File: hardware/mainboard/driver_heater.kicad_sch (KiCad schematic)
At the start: 8 parts, among them J18 Screw_Terminal_01x02, Q1 AGM308MBP, SW9 SW_SPDT

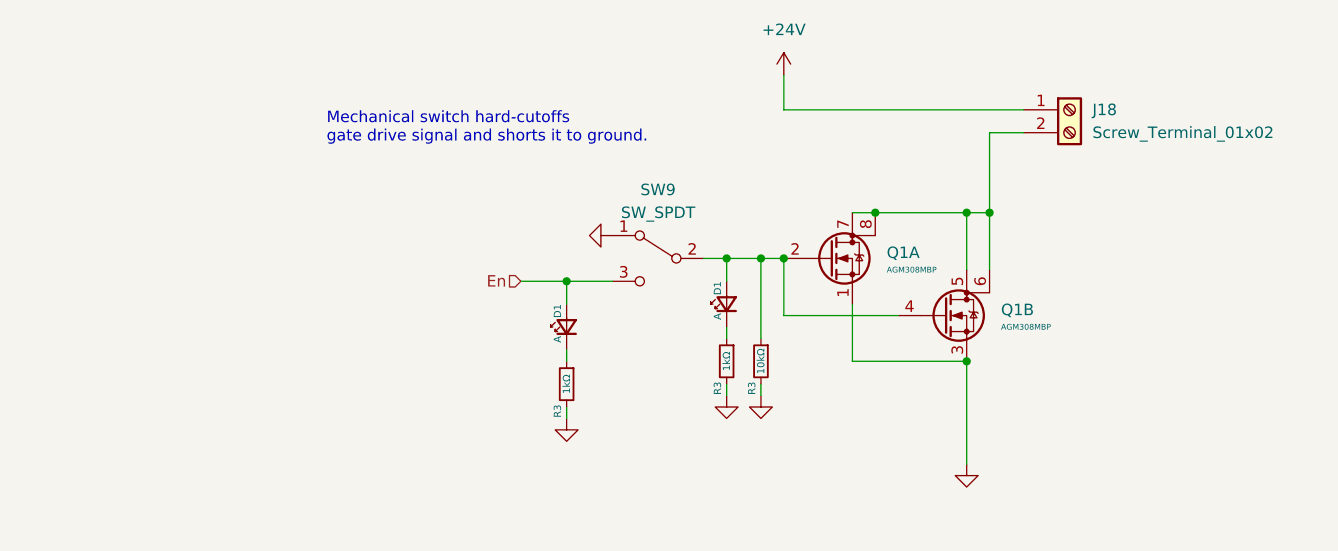
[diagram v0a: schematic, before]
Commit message: saving mainboard, gonna tear out the entire thing and redo in 4-layer
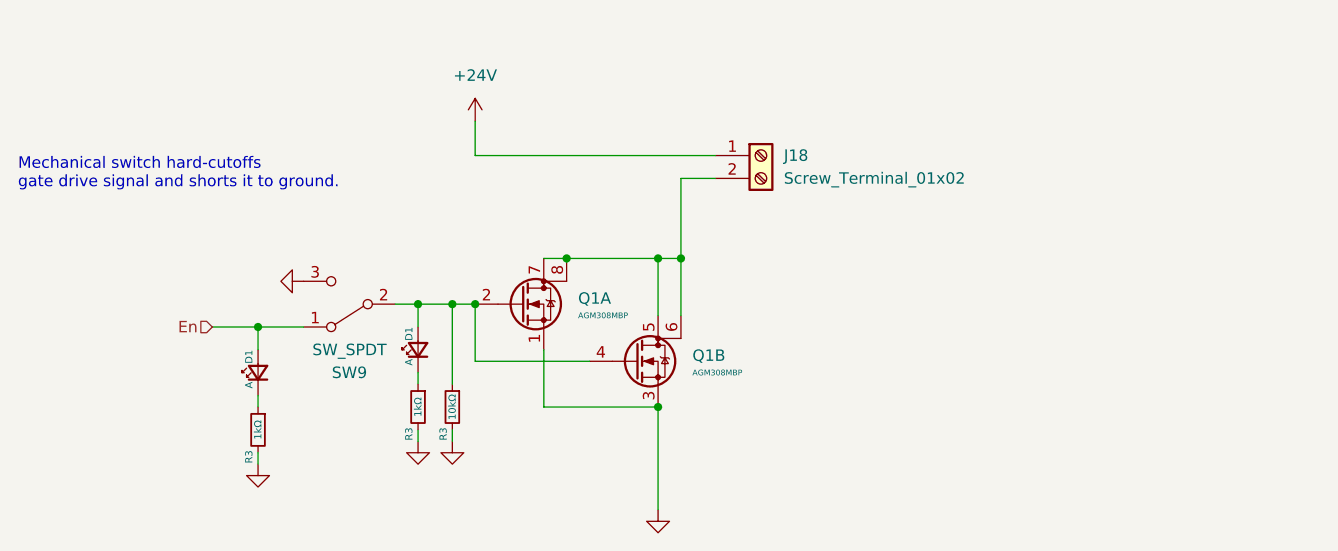
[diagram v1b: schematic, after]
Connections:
- net En: now also SW9.1 (A); no longer SW9.3 (C)
- net GND: now also SW9.3 (C); no longer SW9.1 (A)
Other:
- moved on the sheet: D1, J18, Q1A, Q1B, R3, SW9

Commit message: further board edits, mostly done with power planes, heaters, fans, motor channels, starting work on microcontroller signals
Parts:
- R3: footprint AlphaLib:0603R -> AlphaLib:0402R
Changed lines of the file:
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@@
       (effects (font (size 0.8 0.8)))
     )
-    (property "Footprint" "AlphaLib:0603R" (at 44.45 74.93 0)
+    (property "Footprint" "AlphaLib:0402R" (at 44.45 74.93 0)
       (effects (font (size 1.27 1.27)) hide)
     )
@@
       (effects (font (size 0.8 0.8)))
     )
-    (property "Footprint" "AlphaLib:0603R" (at 66.04 72.39 0)
+    (property "Footprint" "AlphaLib:0402R" (at 66.04 72.39 0)
       (effects (font (size 1.27 1.27)) hide)
     )
@@
       (effects (font (size 0.8 0.8)))
     )
-    (property "Footprint" "AlphaLib:0603R" (at 62.23 72.39 0)
-      (effects (font (size 1.27 1.27)) hide)
-    )
+    (property "Footprint" "AlphaLib:0402R" (at 62.23 72.39 0)
+      (effects (font (size 1.27 1.27)) hide)
+    )

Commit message: redoing board for version alpha 0.2
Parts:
- removed D1 (x2): A, AlphaLib:0603LED, symbol Device:LED_Small
- removed R3 (x2): 1kΩ, AlphaLib:0402R, symbol Device:R_Small
- removed R3: 10kΩ, AlphaLib:0402R, symbol Device:R_Small
- removed SW9: SW_SPDT, corevus:MSS12C02-LS, symbol Switch:SW_SPDT
- added D1: Red, AlphaLib:0402LED, symbol Device:LED_Small
- added R3: 10kΩ, AlphaLib:0402R, symbol Device:R_Small
- added R3: 1kΩ, AlphaLib:0402R, symbol Device:R_Small
- renumbered J18 to J21
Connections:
- net En: now also Q1.2 (G), Q1.4 (G), D1.2 (A), R3.1
- net GND: now also R3.2, R3.2
- new net: D1.1 (K), R3.1
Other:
- moved on the sheet: J21, Q1A

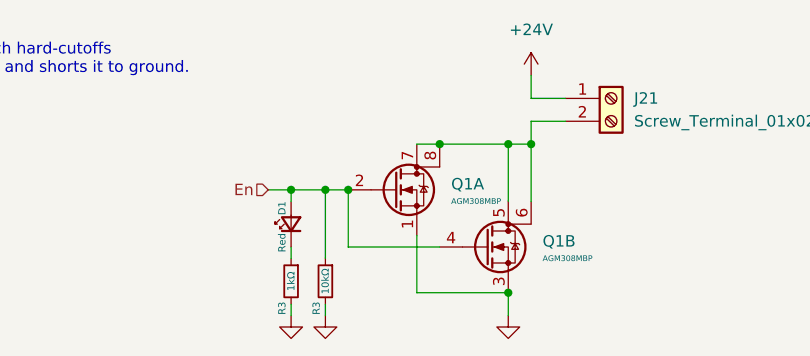
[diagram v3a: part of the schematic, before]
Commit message: tested SMD style XH connectors — didn't work very well alas
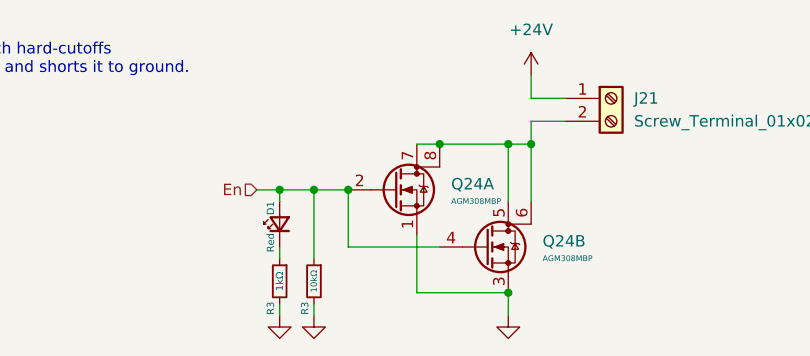
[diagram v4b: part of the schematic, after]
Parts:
- renumbered Q1 to Q24
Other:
- moved on the sheet: D1, R3

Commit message: fan ports
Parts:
- removed Q24: AGM308MBP, corevus:AGM308MBP, symbol Device:Q_Dual_NMOS_S1G1S2G2D2D2D1D1
- removed R3: 10kΩ, AlphaLib:0402R, symbol Device:R_Small
- added Q26: 60N03F, corevus:MOSFET_DFN8, symbol corevus:Q_NMOS-E_Generic_SSSGDDDD
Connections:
- net En: now also Q26.4 (G)
- net GND: now also Q26.1 (S), Q26.2 (S), Q26.3 (S)
- net at J21.2 (Pin_2): now also Q26.5 (D), Q26.6 (D), Q26.7 (D), Q26.8 (D)
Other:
- moved on the sheet: J21
